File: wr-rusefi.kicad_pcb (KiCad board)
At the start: 2 copper layers, 88.9 x 78.7 mm, 142 parts, among them P101 USB_OTG, P102 CONN_01X08, P103 CONN_01X08, P104 CONN_01X04, P105 CONN_01X08, P106 CONN_01X08, P107 CONN_01X02, P108 USB_OTG, P109 CONN_01X02, P110 CONN_01X06, Q401 IRF540N, Q402 IRF540N, Q403 IRF540N, Q404 IRF540N, Q405 IRF540N, Q406 IRF540N, U101 ISL89410, U102 ISL89410, U103 FT230XS, U104 MAX9924, U105 MCP2562-E/SN, U106 LD1117S33TR, U107 MAX9924, U108 ISL89410, U109 STM32F407VGTx, U110 ISL89410, U201 LM324, U301 LM324, U501 LM7805CT, Y101 Crystal

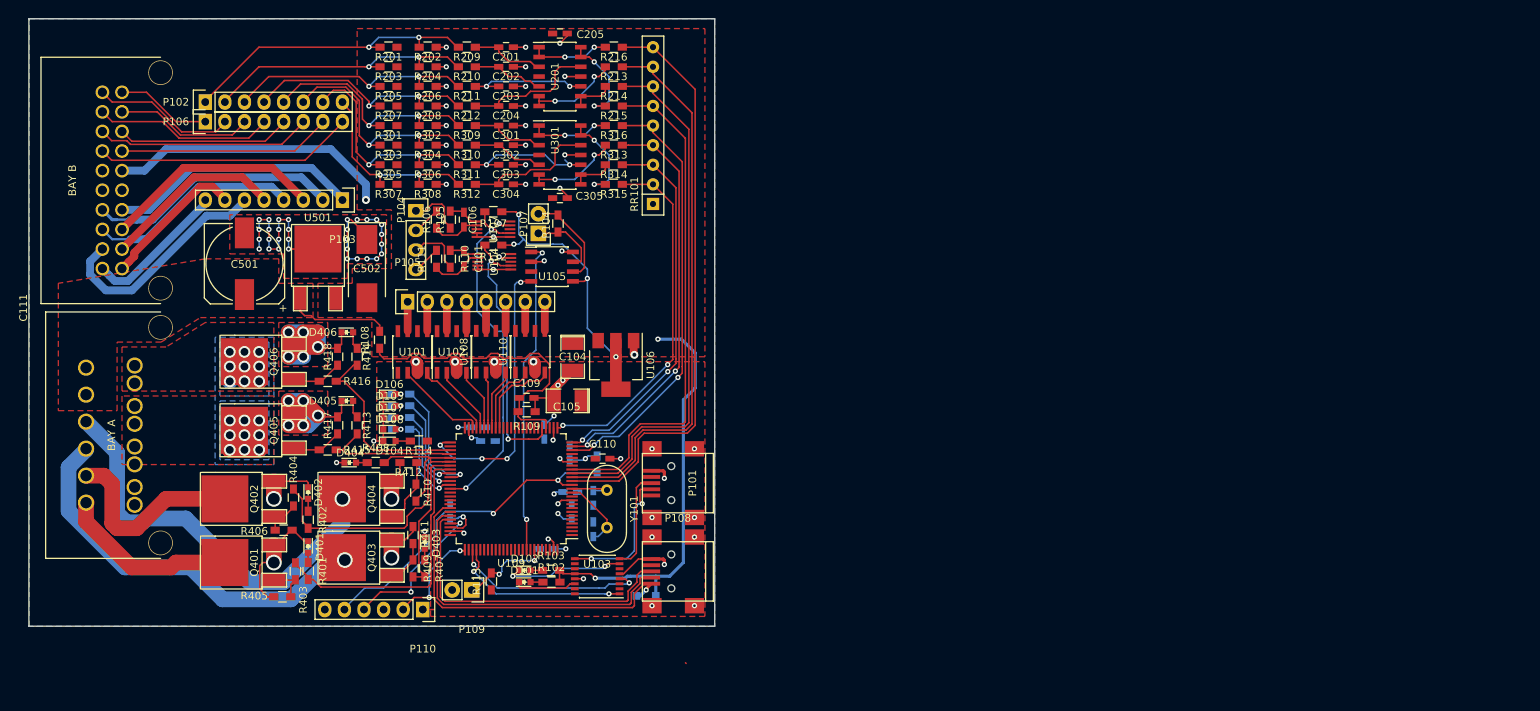
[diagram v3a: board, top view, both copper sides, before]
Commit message: Shrink, place all silk text
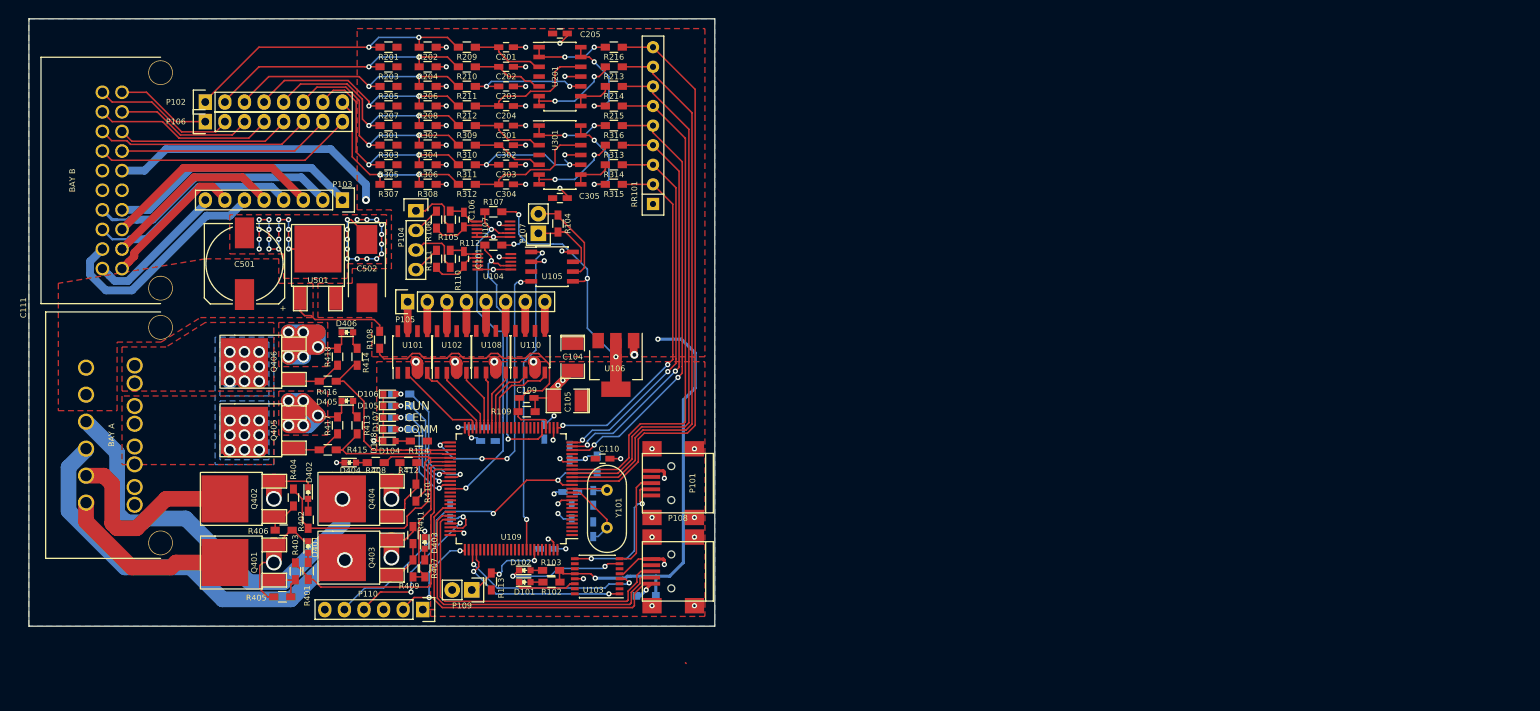
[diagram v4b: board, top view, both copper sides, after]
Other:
- board text added: "CEL"
- board text added: "COMM"
- board text added: "RUN"

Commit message: cleanup
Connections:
- net Net-(C109-Pad1) renamed BATT_ADC
- net Net-(D103-Pad2) renamed VBUS
- net Net-(P108-Pad2) renamed USB_DM
- net Net-(P108-Pad3) renamed USB_DP
- net Net-(P110-Pad2) renamed SWCLK
- net Net-(P110-Pad4) renamed SWDIO

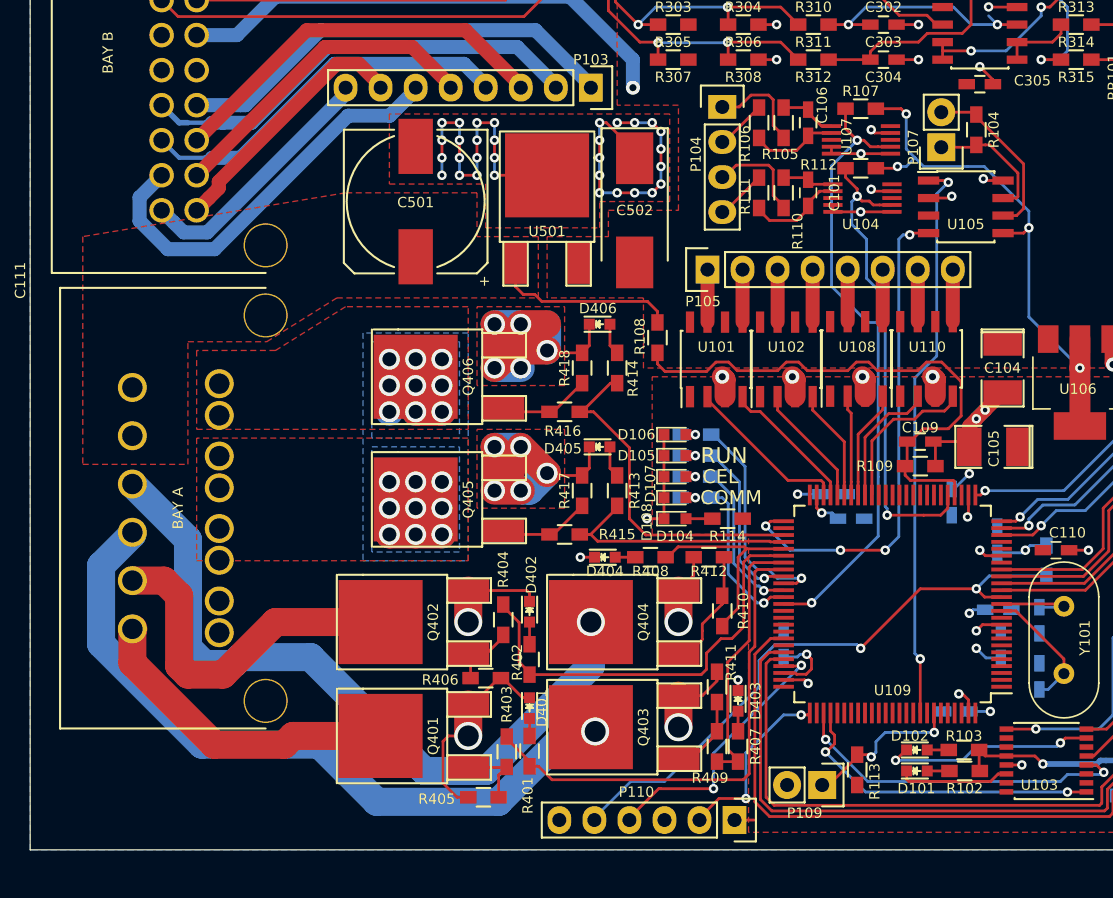
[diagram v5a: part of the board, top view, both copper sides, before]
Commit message: Add reverse protection diode, board cleanup
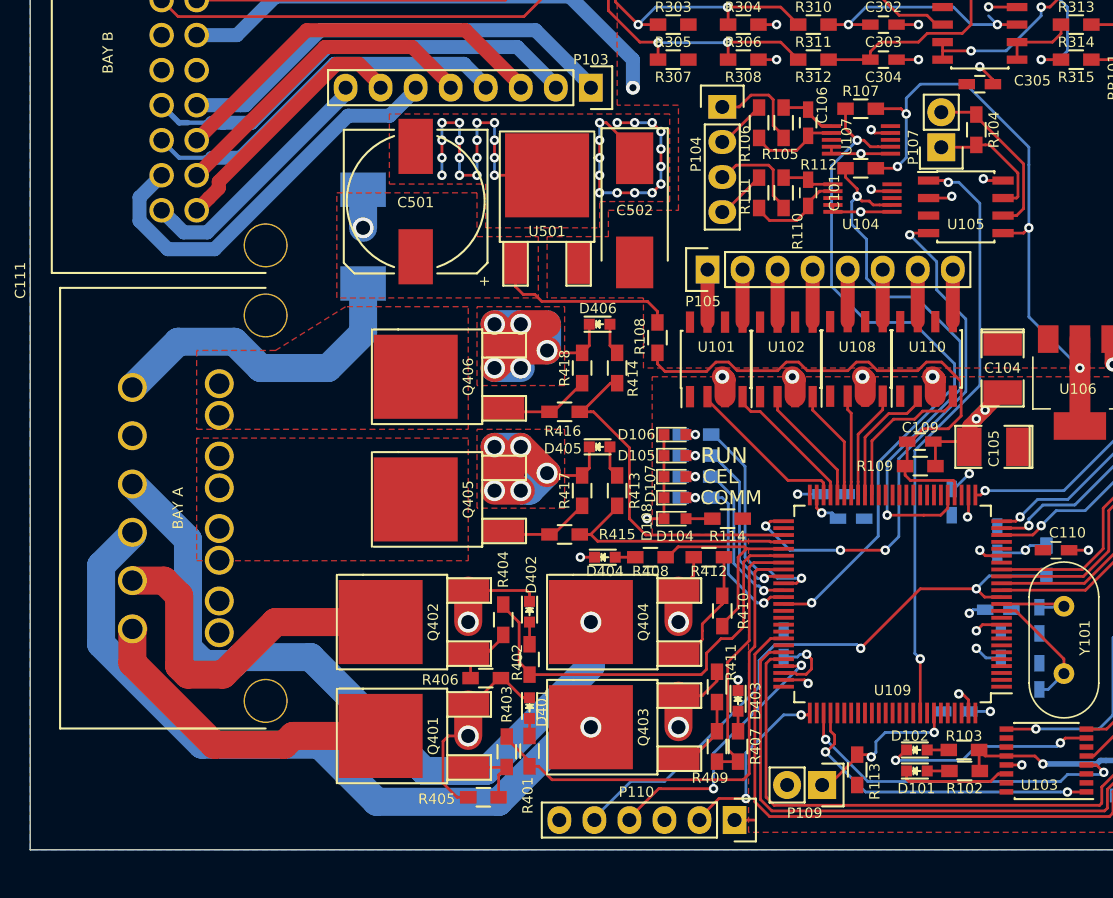
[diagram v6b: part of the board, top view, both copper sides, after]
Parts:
- added D109: D_Schottky, Diodes_SMD:D_SMC_Standard, B.Cu at (92.7, 87.0)
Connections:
- C111 pad 6: +12V -> Net-(C111-Pad6)
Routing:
- net Net-(C111-Pad6): track 0.00 -> 23.5 mm
- net inj_b: track 18.0 -> 2.80 mm, vias 9 -> 0
- net inj_a: track 14.2 -> 0.00 mm, vias 9 -> 0
- net +3V3: track 53.6 -> 59.9 mm
- net VRIN1: track 45.5 -> 51.5 mm
- net VRIN2: track 35.1 -> 40.7 mm
- net CAN_RX: track 36.1 -> 39.2 mm
- net +12V: track 13.6 -> 16.3 mm, vias 0 -> 1
- net CAN_TX: track 41.1 -> 43.5 mm
- removed copper zone on B.Cu, net inj_a
- removed copper zone on B.Cu, net inj_b

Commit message: minor layout
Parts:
- added R119: 5k, Resistors_SMD:R_0805_HandSoldering, F.Cu at (125.2, 85.3)
- added R120: 5k, Resistors_SMD:R_0805_HandSoldering, F.Cu at (130.6, 77.7)
- added R121: 5k, Resistors_SMD:R_0805_HandSoldering, F.Cu at (130.6, 80.3)
- added R122: 5k, Resistors_SMD:R_0805_HandSoldering, F.Cu at (130.6, 82.8)
- R105, R106, R110, R111: value 10k -> 5k; footprint Resistors_SMD:R_0603_HandSoldering -> Resistors_SMD:R_0805_HandSoldering
- moved P107 11.0 mm to (144.8, 84.8)
- moved R104 11.0 mm to (147.3, 83.6)
- moved U105 11.0 mm to (146.6, 89.2)
- moved C101 9.48 mm to (134.4, 85.1)
- moved C106 9.48 mm to (134.4, 80.0)
- moved U104 9.48 mm to (138.3, 85.5)
- moved R107 9.48 mm to (138.2, 79.0)
- moved R112 9.48 mm to (138.2, 83.3)
- moved U107 9.48 mm to (138.2, 81.3)
- moved R111 9.27 mm to (130.6, 85.3), turned to 180 degrees
- moved R106 4.10 mm to (125.2, 80.3), turned to 180 degrees
- moved R105 2.27 mm to (125.2, 77.7), turned to 180 degrees
- moved R110 2.27 mm to (125.2, 82.8), turned to 180 degrees
- moved P104 2.16 mm to (120.9, 77.7)
- moved R108 1.32 mm to (113.0, 93.5)
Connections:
- R105 pad 1: Net-(C106-Pad1) -> Net-(R105-Pad1)
- R106 pad 1: Net-(C106-Pad2) -> Net-(R106-Pad1)
- R110 pad 1: Net-(C101-Pad1) -> Net-(R110-Pad1)
- R111 pad 2: VR2- -> Net-(R111-Pad2)
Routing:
- net VRIN1: track 51.5 -> 43.9 mm
- net VRIN2: track 40.7 -> 36.2 mm
- net VR1+: track 7.27 -> 2.97 mm
- net VR2+: track 7.27 -> 2.97 mm
- net CAN_RX: track 39.2 -> 35.7 mm
- net +3V3: track 59.9 -> 63.3 mm, vias 10 -> 9
- net Net-(R111-Pad2): track 0.00 -> 2.63 mm
- net Net-(R110-Pad1): track 0.00 -> 2.63 mm
- net Net-(R106-Pad1): track 0.00 -> 2.63 mm
- net Net-(R105-Pad1): track 0.00 -> 2.63 mm
- net CAN_TX: track 43.5 -> 41.4 mm
- net BATT_ADC: track 39.9 -> 41.8 mm
- net Net-(C101-Pad2): track 6.96 -> 5.12 mm
- net +12V: track 16.3 -> 14.5 mm
- net Net-(C106-Pad2): track 6.36 -> 4.53 mm
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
